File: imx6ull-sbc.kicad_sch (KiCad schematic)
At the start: 0 parts

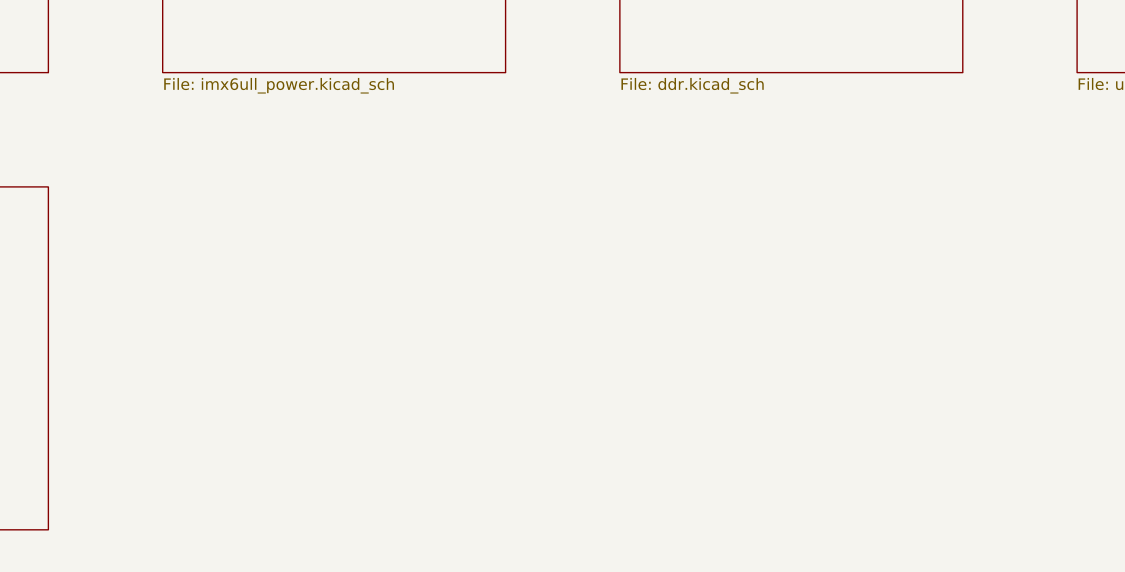
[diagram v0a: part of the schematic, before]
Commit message: more ddr routing, add more connectors
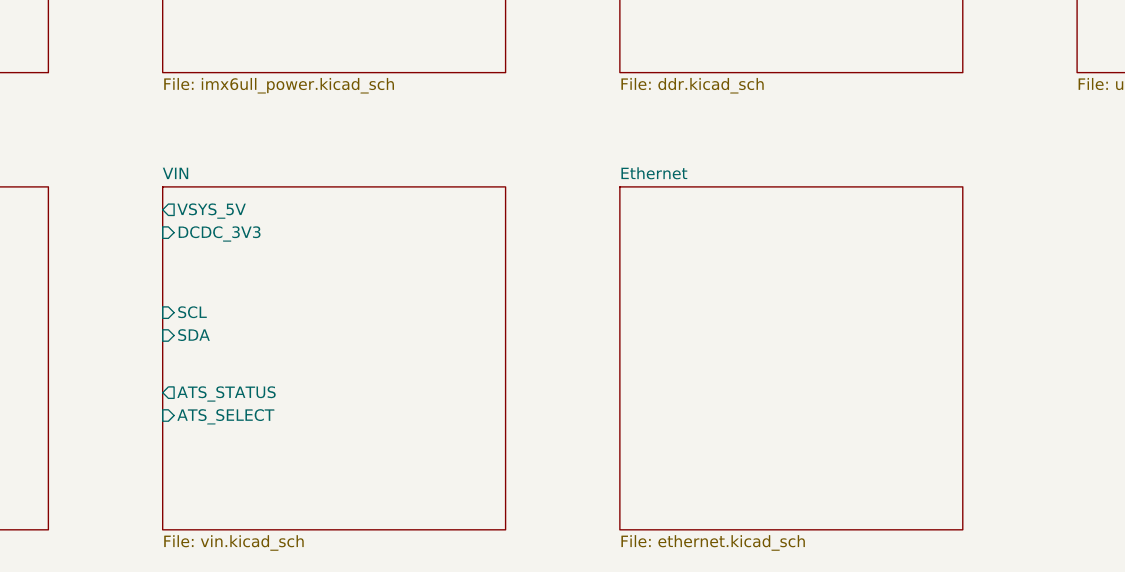
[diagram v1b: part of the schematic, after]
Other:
- added sheet Ethernet (ethernet.kicad_sch)
- added sheet VIN (vin.kicad_sch)

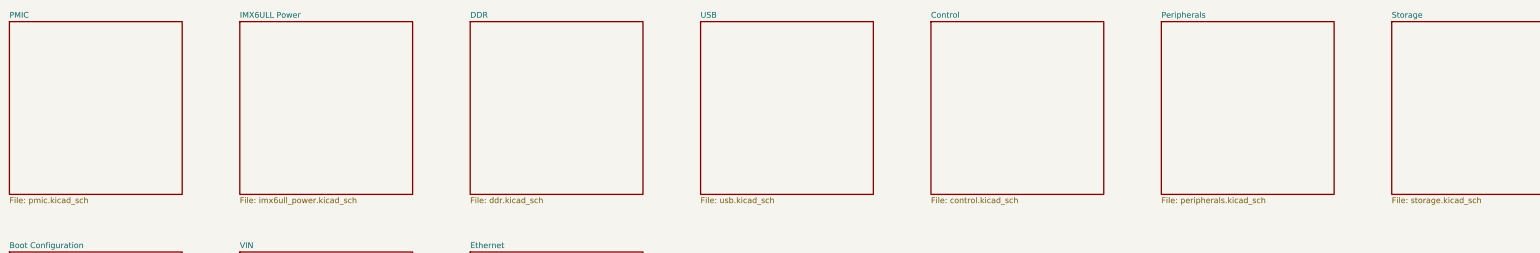
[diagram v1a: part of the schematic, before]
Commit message: start moving to hierarchal labels, add emmc
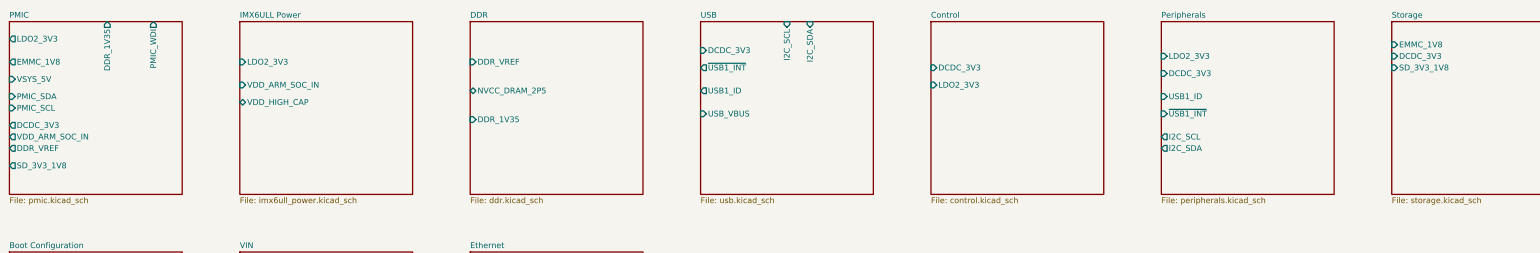
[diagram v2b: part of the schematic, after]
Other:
- sheet Control ports: added DCDC_3V3, LDO2_3V3; removed none
- sheet DDR ports: added DDR_1V35, DDR_VREF, NVCC_DRAM_2P5; removed none
- sheet IMX6ULL Power ports: added LDO2_3V3, VDD_ARM_SOC_IN, VDD_HIGH_CAP; removed none
- sheet PMIC ports: added DCDC_3V3, DDR_1V35, DDR_VREF, EMMC_1V8, LDO2_3V3, PMIC_SCL, PMIC_SDA, PMIC_WDI, SD_3V3_1V8, VDD_ARM_SOC_IN, VSYS_5V; removed none
- sheet Peripherals ports: added DCDC_3V3, I2C_SCL, I2C_SDA, LDO2_3V3, USB1_ID, ~{USB1_INT}; removed none
- sheet Storage ports: added DCDC_3V3, EMMC_1V8, SD_3V3_1V8; removed none
- sheet USB ports: added DCDC_3V3, I2C_SCL, I2C_SDA, USB1_ID, USB_VBUS, ~{USB1_INT}; removed none
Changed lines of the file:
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@@
       (effects (font (size 1.27 1.27)) (justify left top))
+    )
+    (pin "LDO2_3V3" input (at 292.1 58.42 180)
+      (effects (font (size 1.27 1.27)) (justify left))
+    )
+    (pin "DCDC_3V3" input (at 292.1 62.23 180)
+      (effects (font (size 1.27 1.27)) (justify left))
+    )
+    (pin "USB1_ID" input (at 292.1 67.31 180)
+      (effects (font (size 1.27 1.27)) (justify left))
+    )
+    (pin "~{USB1_INT}" input (at 292.1 71.12 180)
+      (effects (font (size 1.27 1.27)) (justify left))
+    )
+    (pin "I2C_SCL" output (at 292.1 76.2 180)
+      (effects (font (size 1.27 1.27)) (justify left))
+    )
+    (pin "I2C_SDA" output (at 292.1 78.74 180)
+      (effects (font (size 1.27 1.27)) (justify left))
     )
   )
@@
       (effects (font (size 1.27 1.27)) (justify left top))
     )
+    (pin "DCDC_3V3" input (at 190.5 57.15 180)
+      (effects (font (size 1.27 1.27)) (justify left))
+    )
+    (pin "~{USB1_INT}" output (at 190.5 60.96 180)
+      (effects (font (size 1.27 1.27)) (justify left))
+    )
+    (pin "USB1_ID" output (at 190.5 66.04 180)
+      (effects (font (size 1.27 1.27)) (justify left))
+    )
+    (pin "USB_VBUS" input (at 190.5 71.12 180)
+      (effects (font (size 1.27 1.27)) (justify left))
+    )
+    (pin "I2C_SCL" input (at 209.55 50.8 90)
+      (effects (font (size 1.27 1.27)) (justify right))
+    )
+    (pin "I2C_SDA" input (at 214.63 50.8 90)
+      (effects (font (size 1.27 1.27)) (justify right))
+    )
   )
   (sheet (at 38.1 50.8) (size 38.1 38.1) (fields_autoplaced)
@@
       (effects (font (size 1.27 1.27)) (justify left top))
     )
+    (pin "VSYS_5V" input (at 38.1 63.5 180)
+      (effects (font (size 1.27 1.27)) (justify left))
+    )
+    (pin "PMIC_SDA" input (at 38.1 67.31 180)
+      (effects (font (size 1.27 1.27)) (justify left))
+    )
+    (pin "PMIC_SCL" input (at 38.1 69.85 180)
+      (effects (font (size 1.27 1.27)) (justify left))
+    )
+    (pin "DCDC_3V3" output (at 38.1 73.66 180)
+      (effects (font (size 1.27 1.27)) (justify left))
+    )
+    (pin "EMMC_1V8" output (at 38.1 59.69 180)
+      (effects (font (size 1.27 1.27)) (justify left))
+    )
+    (pin "SD_3V3_1V8" output (at 38.1 82.55 180)
+      (effects (font (size 1.27 1.27)) (justify left))
+    )
+    (pin "LDO2_3V3" output (at 38.1 54.61 180)
+      (effects (font (size 1.27 1.27)) (justify left))
+    )
+    (pin "DDR_VREF" output (at 38.1 78.74 180)
+      (effects (font (size 1.27 1.27)) (justify left))
+    )
+    (pin "VDD_ARM_SOC_IN" output (at 38.1 76.2 180)
+      (effects (font (size 1.27 1.27)) (justify left))
+    )
+    (pin "DDR_1V35" output (at 59.69 50.8 90)
+      (effects (font (size 1.27 1.27)) (justify right))
+    )
+    (pin "PMIC_WDI" output (at 69.85 50.8 90)
+      (effects (font (size 1.27 1.27)) (justify right))
+    )
   )
   (sheet (at 88.9 50.8) (size 38.1 38.1) (fields_autoplaced)
@@
       (effects (font (size 1.27 1.27)) (justify left top))
     )
+    (pin "LDO2_3V3" input (at 88.9 59.69 180)
+      (effects (font (size 1.27 1.27)) (justify left))
+    )
+    (pin "VDD_ARM_SOC_IN" input (at 88.9 64.77 180)
+      (effects (font (size 1.27 1.27)) (justify left))
+    )
+    (pin "VDD_HIGH_CAP" bidirectional (at 88.9 68.58 180)
+      (effects (font (size 1.27 1.27)) (justify left))
+    )
   )
   (sheet (at 38.1 101.6) (size 38.1 38.1) (fields_autoplaced)
@@
       (effects (font (size 1.27 1.27)) (justify left top))
     )
+    (pin "DDR_VREF" input (at 139.7 59.69 180)
+      (effects (font (size 1.27 1.27)) (justify left))
+    )
+    (pin "NVCC_DRAM_2P5" bidirectional (at 139.7 66.04 180)
+      (effects (font (size 1.27 1.27)) (justify left))
+    )
+    (pin "DDR_1V35" input (at 139.7 72.39 180)
+      (effects (font (size 1.27 1.27)) (justify left))
+    )
   )
   (sheet (at 342.9 50.8) (size 38.1 38.1) (fields_autoplaced)
@@
       (effects (font (size 1.27 1.27)) (justify left top))
     )
+    (pin "EMMC_1V8" input (at 342.9 55.88 180)
+      (effects (font (size 1.27 1.27)) (justify left))
+    )
+    (pin "DCDC_3V3" input (at 342.9 58.42 180)
+      (effects (font (size 1.27 1.27)) (justify left))
+    )
+    (pin "SD_3V3_1V8" input (at 342.9 60.96 180)
+      (effects (font (size 1.27 1.27)) (justify left))
+    )
   )
   (sheet (at 241.3 50.8) (size 38.1 38.1) (fields_autoplaced)
@@
     (property "Sheet file" "control.kicad_sch" (id 1) (at 241.3 89.4846 0)
       (effects (font (size 1.27 1.27)) (justify left top))
+    )
+    (pin "DCDC_3V3" input (at 241.3 60.96 180)
+      (effects (font (size 1.27 1.27)) (justify left))
+    )
+    (pin "LDO2_3V3" input (at 241.3 64.77 180)
+      (effects (font (size 1.27 1.27)) (justify left))
     )
   )
@@
       (reference "J6") (unit 1) (value "CRJ011-ML3-TH") (footprint "imx6ull-sbc:CUI_CRJ011-ML3-TH")
     )
+    (path "/ee098d98-1bdc-4eef-8201-e0a7ac56e4cd/e87822bc-3ff3-4a00-b56a-8b436ba737e8"
+      (reference "J?") (unit 1) (value "Conn_01x06_Male") (footprint "")
+    )
     (path "/8526cf4d-dcc1-4418-b051-6f5b18e2eade/6b595e14-90a8-440b-ad03-8290c07cc855"
       (reference "L1") (unit 1) (value "1uH") (footprint "Inductor_SMD:L_0603_1608Metric")
@@
       (reference "R15") (unit 1) (value "10K") (footprint "Resistor_SMD:R_0402_1005Metric")
     )
-    (path "/ed3c1fe6-129f-450c-8aa8-14886c123fc5/e51424d7-e4d2-4647-8967-442e0efa73ff"
-      (reference "R16") (unit 1) (value "10R") (footprint "Resistor_SMD:R_0402_1005Metric")
-    )
     (path "/ed3c1fe6-129f-450c-8aa8-14886c123fc5/e067f1e8-c9ef-4d55-be3b-4d732d5c340c"
       (reference "R17") (unit 1) (value "10K") (footprint "Resistor_SMD:R_0402_1005Metric")
@@
       (reference "U9") (unit 1) (value "W25Q32JVZP") (footprint "Package_SON:WSON-8-1EP_6x5mm_P1.27mm_EP3.4x4.3mm")
     )
-    (path "/ed3c1fe6-129f-450c-8aa8-14886c123fc5/674ecf48-46ed-467d-8fe7-d5b7baec47fc"
-      (reference "U10") (unit 1) (value "SFEM064GB1ED1TO-I-6F-111-STD") (footprint "imx6ull-sbc:BGA153N50P14X14_1150X1300X100")
+    (path "/ed3c1fe6-129f-450c-8aa8-14886c123fc5/7844d524-639d-4517-971c-7d9be5ef95f9"
+      (reference "U10") (unit 1) (value "SFEM064GB1ED1TO-I-6F-111-STD") (footprint "imx6ull-sbc:FBGA-153")
     )
     (path "/71ff8a8a-f2b3-47ad-800a-46f18039bb8e/9ef44b3d-6686-4866-a167-c2655a3955e9"
@@
       (reference "U18") (unit 1) (value "DP83825IRMQR") (footprint "imx6ull-sbc:XCVR_DP83825IRMQR")
     )
+    (path "/8526cf4d-dcc1-4418-b051-6f5b18e2eade/d47b476a-86f2-4b4f-bdd6-e2e3aa701a26"
+      (reference "U?") (unit 1) (value "TLV62569DDC") (footprint "Package_TO_SOT_SMD:SOT-23-6")
+    )
+    (path "/ed3c1fe6-129f-450c-8aa8-14886c123fc5/9a9639fe-805e-45cd-8c47-b3e202c87e3c"
+      (reference "U?") (unit 2) (value "SFEM064GB1ED1TO-I-6F-111-STD") (footprint "")
+    )
     (path "/ee098d98-1bdc-4eef-8201-e0a7ac56e4cd/85d8bc65-114a-4a45-8802-f9695120405a"

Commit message: move to hierarchal labels, work on power tree, add basic pcb layout
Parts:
- added H1, H2, H3, H4: MountingHole_Pad, MountingHole:MountingHole_3.2mm_M3_Pad_Via, symbol Mechanical:MountingHole_Pad
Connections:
- new net GND: H1.1, H2.1, H3.1, H4.1
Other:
- sheet PMIC renamed Power
- removed sheet Boot Configuration
- sheet Control ports: added ATS_STATUS, GPIO_DVFS, PMIC_ON_REQ, PMIC_STBY_REQ, SNVS_3V3; removed LDO2_3V3
- sheet DDR ports: added none; removed DDR_VREF
- sheet Ethernet ports: added DCDC_3V3; removed none
- sheet IMX6ULL Power ports: added DCDC_3V3, LDO_3V3, SNVS_3V3; removed LDO2_3V3
- sheet Peripherals ports: added I2C1_SCL, I2C1_SDA, LDO_3V3, SD1_VSELECT, ~{WDOG}; removed I2C_SCL, I2C_SDA, LDO2_3V3
- sheet Power: file pmic.kicad_sch -> power.kicad_sch
- sheet Power ports: added LDO_1V8, LDO_3V3, SD1_VSELECT, SNVS_3V3, VDD_SNVS_3V3, ~{WDOG}; removed DDR_VREF, EMMC_1V8, LDO2_3V3, PMIC_SCL, PMIC_SDA, PMIC_WDI
- sheet VIN ports: added I2C_SCL, I2C_SDA; removed ATS_SELECT, SCL, SDA
- note added: "Temp Fix (X) for Buggy Net Names"

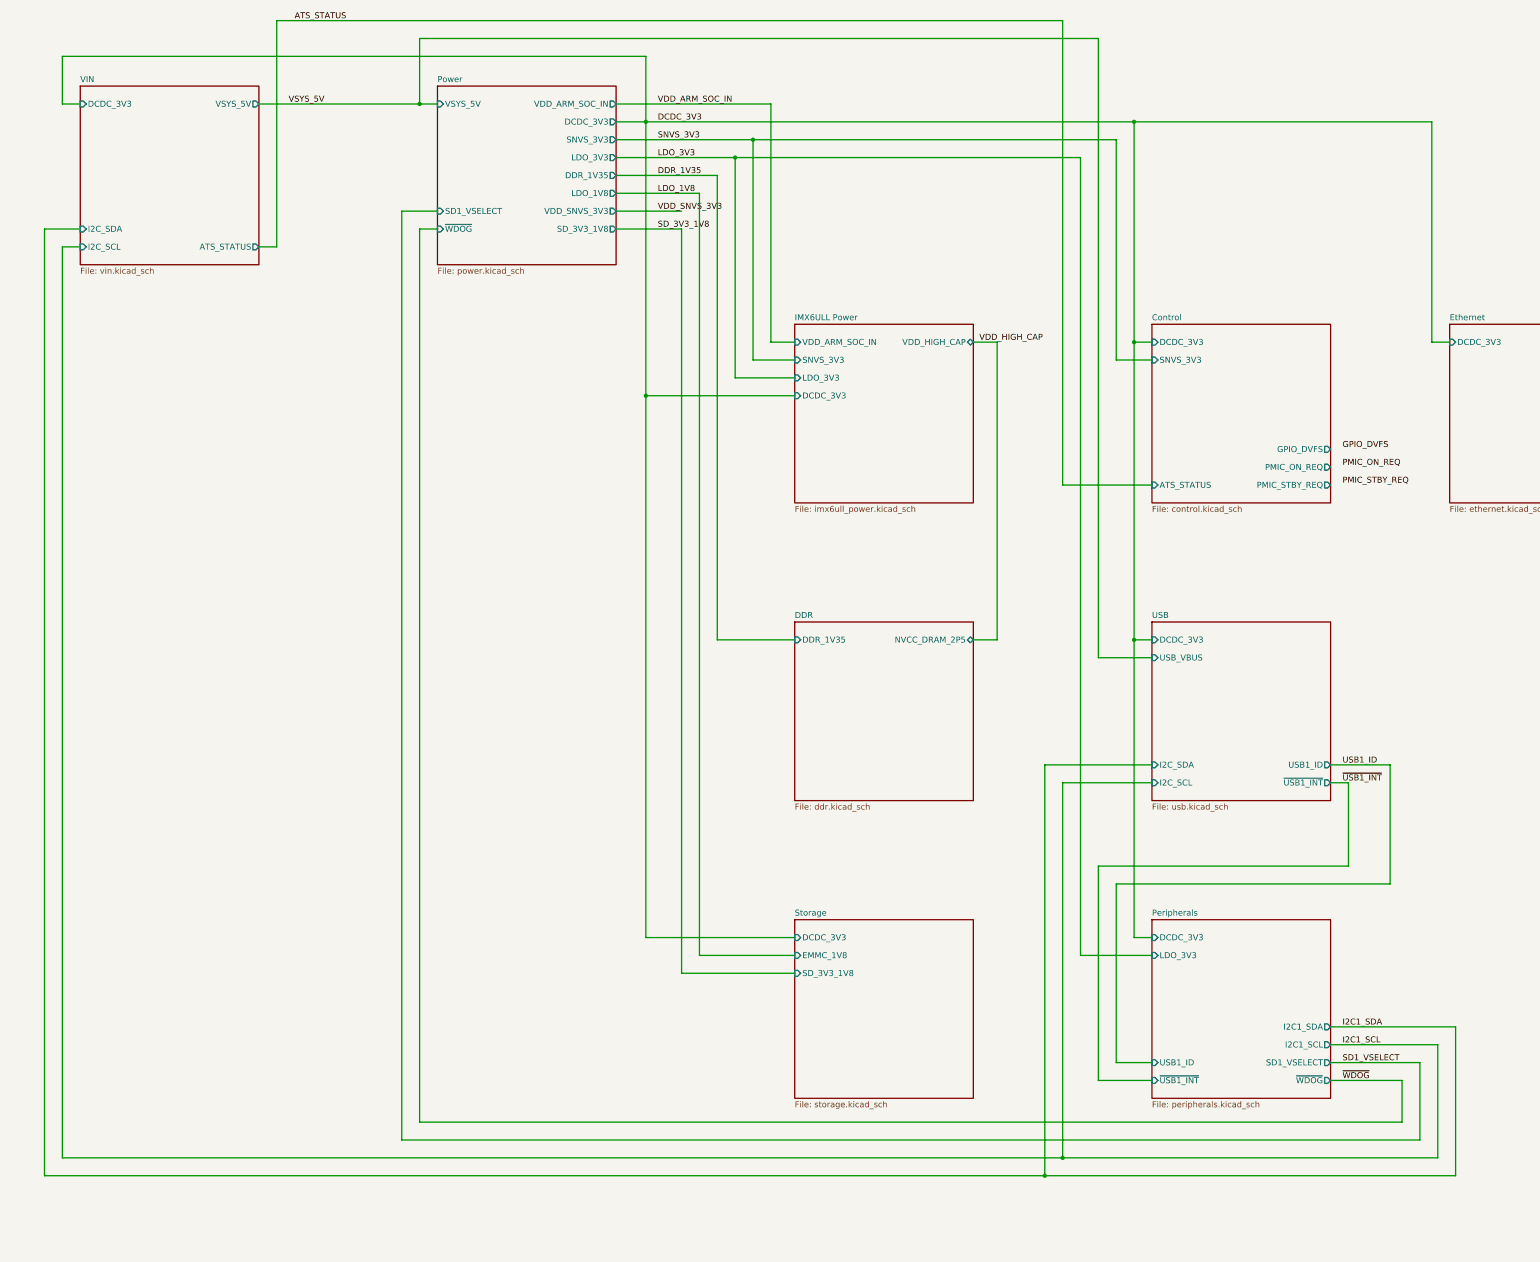
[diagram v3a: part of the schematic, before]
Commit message: most of sch done, inital component pcb placement
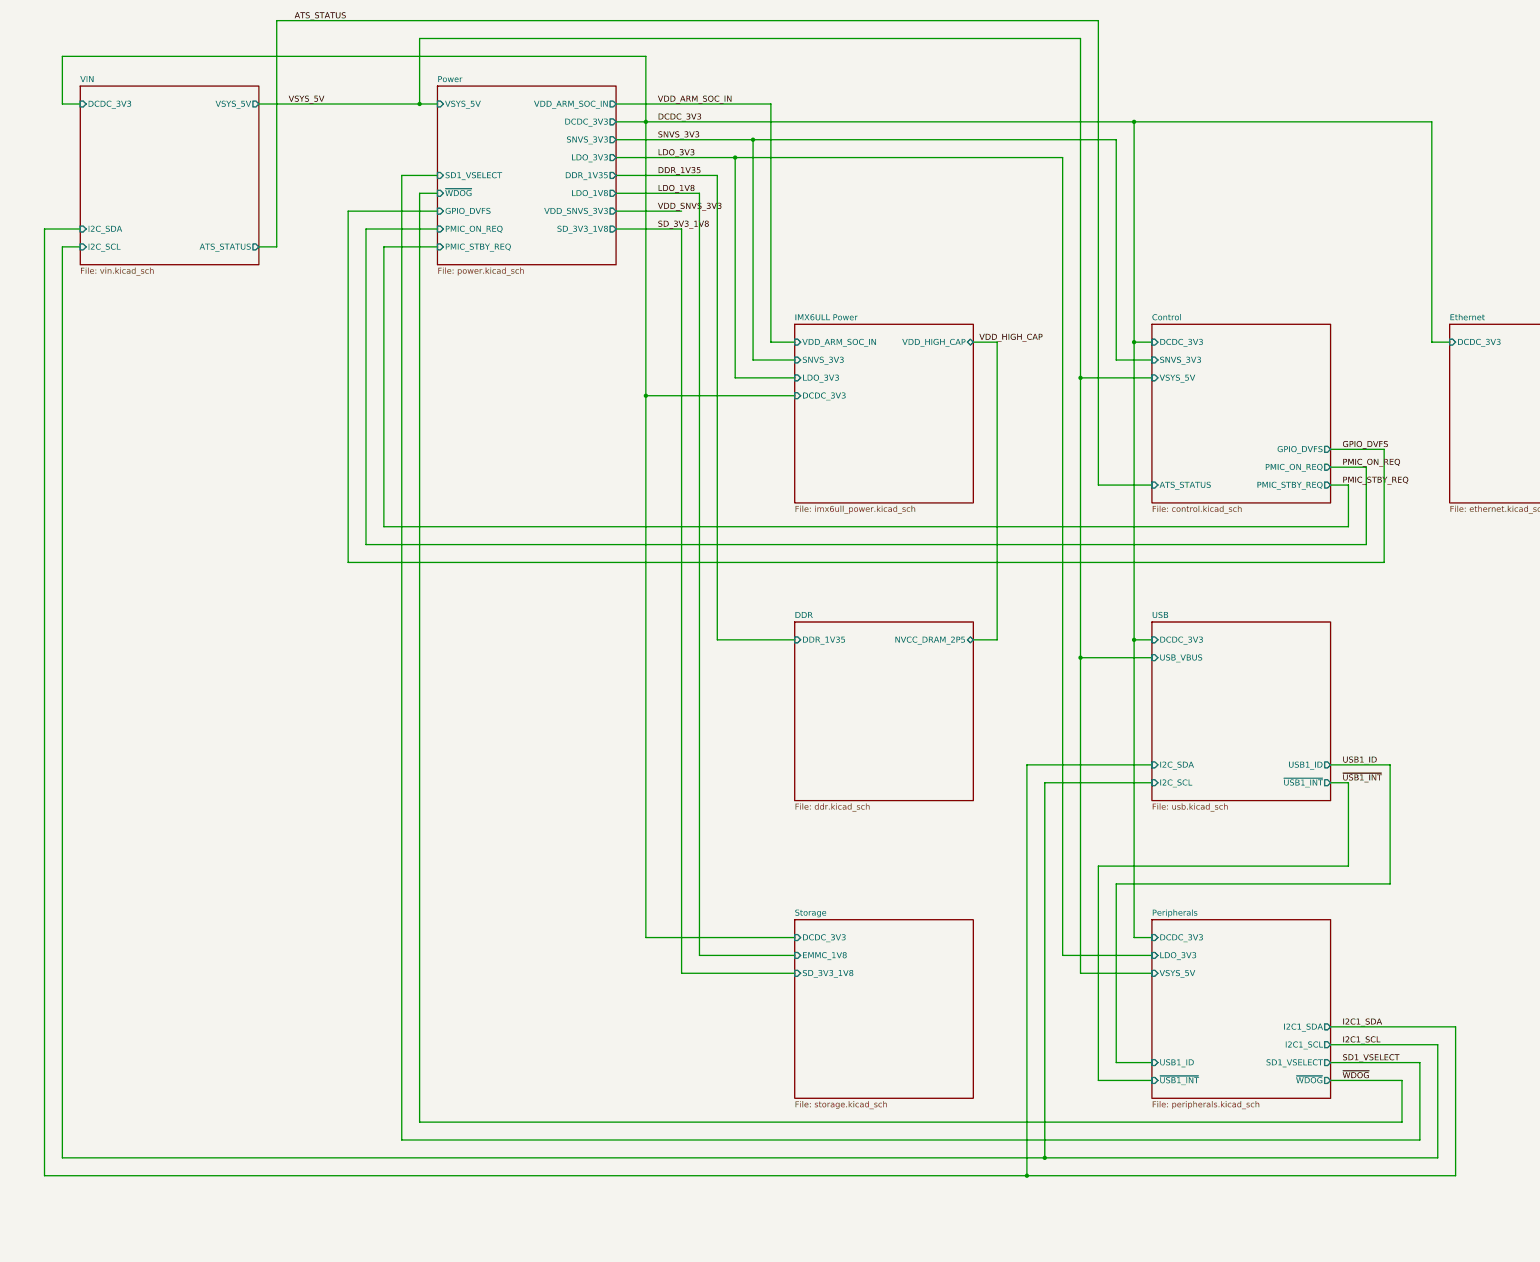
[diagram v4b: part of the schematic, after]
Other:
- sheet Control ports: added VSYS_5V; removed none
- sheet Peripherals ports: added VSYS_5V; removed none
- sheet Power ports: added GPIO_DVFS, PMIC_ON_REQ, PMIC_STBY_REQ; removed none
